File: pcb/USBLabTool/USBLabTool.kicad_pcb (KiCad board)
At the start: 4 copper layers, 79.4 x 56.2 mm, 227 parts, among them J1 Conn_01x06_Pin, J17 2x01, J19 T_N5V, J2 Conn_02x12_Odd_Even, J20 USB_C_Receptacle, K1 G5V-2, K2 G5V-2, Q1 STL11N3LLH6, SW1 TS02-66-73-BK-100-SCR-D, U1 AQY284SX, U10 MC33274ADR2G, U11 DG403, U12 STM32H562VGTx, U13 R1283K002A, U14 ST1L05APU33R, U15 ST1L05APU33R, U16 LTC1983ES6-5TRMPBF, U17 TCPP01-M12, U18 74HC245, U19 USBLC6-2SC6, U2 AQY284SX, U20 74HC245, U3 CD74HC4316, U4 LMP7718, U5 CD74HC4316, U6 LMP7718, U7 OPA863, U8 OPA863, U9 MC33274ADR2G, Y1 32.768kHz, Y2 NX2016SA-25M-EXS00A-CS08742

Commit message: push new layout
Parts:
- added JP3: SJ, Jumper:SolderJumper-2_P1.3mm_Open_RoundedPad1.0x1.5mm, F.Cu at (78.8, 90.0)
- added JP4: SJ, Jumper:SolderJumper-2_P1.3mm_Open_RoundedPad1.0x1.5mm, F.Cu at (74.1, 98.0)
- added JP5: SJ, Jumper:SolderJumper-2_P1.3mm_Open_RoundedPad1.0x1.5mm, F.Cu at (74.0, 95.3)
- added JP6: SJ, Jumper:SolderJumper-2_P1.3mm_Open_RoundedPad1.0x1.5mm, F.Cu at (196.4, 86.9)
- added JP7: SJ, Jumper:SolderJumper-2_P1.3mm_Open_RoundedPad1.0x1.5mm, F.Cu at (196.4, 90.5)
- added R82: 0, Resistor_SMD:R_0603_1608Metric_Pad0.98x0.95mm_HandSolder, F.Cu at (200.8, 86.4)
- added R83: 0, Resistor_SMD:R_0603_1608Metric_Pad0.98x0.95mm_HandSolder, F.Cu at (200.8, 88.9)
- C10, C11, C14, C22, C24, C26, C28, C31, C32, C35, C36, C37, C38, C40, C42, C45, C47, C50, C51, C54, C57, C58, C63, C64, C65, C67, C68, C71, C74, C75, C9, CR2, D10, D4, D5, D6, D9, L7, L8, R11, R13, R14, R15, R16, R17, R18, R19, R20, R23, R32, R35, R37, R56, R57, R59, R60, R61, R65, R68, R69, R70, R71, R72, R73, R74, R75, R76, R77, R78, R79, R80, R81, R9, U1, U13, U14, U15, U17, U19, U3, U8, Y1: moved to F.Cu
- C29, C3, C43, C44, C49, D1, R33, R43, R44, R45, R46, R49, R50, R52, U12: moved to B.Cu
- moved L6 128.7 mm to (58.4, 112.7), turned to 0 degrees
- moved H2 107.6 mm to (198.7, 53.7)
- moved R8 104.9 mm to (86.8, 131.2), turned to 90 degrees
- moved C8 102.9 mm to (88.3, 131.2), turned to -90 degrees
- moved C7 102.7 mm to (89.8, 131.2), turned to 90 degrees
- moved R7 102.1 mm to (91.3, 131.2), turned to -90 degrees
- moved C6 99.6 mm to (94.9, 131.2), turned to -90 degrees
- moved C5 99.4 mm to (98.0, 131.2), turned to 90 degrees
- moved C63 99.3 mm to (85.5, 95.8), turned to -90 degrees
- moved C62 99.2 mm to (89.7, 98.6), turned to 0 degrees
- moved R6 99.0 mm to (96.4, 131.2), turned to -90 degrees
- moved D2 98.9 mm to (108.6, 138.1), turned to -90 degrees
- moved J19 98.4 mm to (82.1, 97.2)
- moved C64 97.6 mm to (86.2, 98.5), turned to 0 degrees
- moved R5 97.2 mm to (99.5, 131.2), turned to 90 degrees
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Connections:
- C33 pad 1: RCC_OSC_IN -> Net-(JP6-B)
- C34 pad 2: RCC_OSC_OUT -> Net-(JP7-A)
- C35 pad 2: RCC_OSC32_IN -> Net-(C35-Pad2)
- C36 pad 2: RCC_OSC32_OUT -> Net-(C36-Pad2)
- C70 pad 1: +5V -> Net-(D10-A)
- C72 pad 2: UCPD_CC1 -> Net-(J20-CC1)
- C73 pad 2: UCPD_CC2 -> Net-(J20-CC2)
- C74 pad 2: +5V -> Net-(D10-A)
- D10 pad 2: +5V -> Net-(D10-A)
- D3 pad 1: +3.3VA -> GNDA
- D3 pad 2: GNDA -> +3.3VA
- D4 pad 1: +3.3VA -> GNDA
- D4 pad 2: GNDA -> +3.3VA
- D9 pad C: +5V -> Net-(D10-A)
- J20 pad A4: +5V -> Net-(D10-A)
- J20 pad A5: UCPD_CC1 -> Net-(J20-CC1)
- J20 pad A9: +5V -> Net-(D10-A)
- J20 pad B4: +5V -> Net-(D10-A)
- J20 pad B5: UCPD_CC2 -> Net-(J20-CC2)
- J20 pad B9: +5V -> Net-(D10-A)
- Q1 pad 5: +5V -> Net-(D10-A)
- R67 pad 1: +5V -> Net-(D10-A)
- U12 pad 70: USB_D- -> USB_FN_N
- U12 pad 71: USB_D+ -> USB_FN_P
- U17 pad 7: UCPD_CC1 -> Net-(J20-CC1)
- U17 pad 9: UCPD_CC2 -> Net-(J20-CC2)
- Y1 pad 1: RCC_OSC32_OUT -> Net-(C36-Pad2)
- Y1 pad 2: RCC_OSC32_IN -> Net-(C35-Pad2)
- Y2 pad 1: RCC_OSC_IN -> Net-(JP6-B)
- Y2 pad 3: RCC_OSC_OUT -> Net-(JP7-A)
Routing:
- net +5V: track 252.2 -> 78.0 mm, vias 11 -> 6
- net GNDA: track 331.4 -> 181.8 mm, vias 26 -> 14
- net GND: track 272.4 -> 157.4 mm, vias 32 -> 16
- net +3.3V: track 141.5 -> 31.2 mm, vias 11 -> 2
- net NRST: track 86.7 -> 0.00 mm, vias 2 -> 0
- net -5VCLEAN: track 108.1 -> 31.5 mm
- net +5VCLEAN: track 94.1 -> 33.4 mm, vias 7 -> 4
- net C0_IN: track 53.1 -> 4.65 mm, vias 2 -> 0
- net CH0_ACDC: track 45.9 -> 1.32 mm, vias 3 -> 1
- net +12VA: track 81.2 -> 40.0 mm, vias 5 -> 2
- net UCPD_FLT: track 42.7 -> 2.58 mm, vias 4 -> 1
- net P_CH0_IN: track 51.7 -> 11.9 mm
- net USB_D-: track 50.6 -> 11.9 mm, vias 4 -> 2
- net -12VA: track 75.0 -> 37.2 mm, vias 9 -> 5
- net UCPD_CC2: track 55.7 -> 19.2 mm, vias 5 -> 2
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- removed copper zone on In1.Cu, net GND
- removed copper zone on In1.Cu, net GNDA
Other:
- board outline removed
- board text removed: "ECE USB Multi-Function Lab Instrument"
- board text removed: "RESET"

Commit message: pcb update
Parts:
- turned GD2 to 180 degrees
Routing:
- net P_CH0_IN: track 11.9 -> 0.00 mm
- net Net-(C7-Pad2): track 9.14 -> 16.8 mm
- net GNDA: track 181.8 -> 175.1 mm, vias 14 -> 13
- net Net-(C7-Pad1): track 4.29 -> 5.83 mm
- net /AWG_FrontEnd/C1_OUT_G: track 16.5 -> 15.5 mm
- net /AWG_FrontEnd/C0_FB: track 25.5 -> 24.8 mm
- net Net-(U11B-D2): track 7.71 -> 7.15 mm

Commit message: pcb updates
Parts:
- turned GD1 to 180 degrees
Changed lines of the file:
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@@
 	(footprint "userfp:GDT_SH_LTF"
 		(layer "F.Cu")
-		(at 125.8715 139.7615)
+		(at 125.8715 139.7615 180)
 		(tags "SH90 ")
 		(property "Reference" "GD1"
-			(at 0 0 0)
+			(at 0 0 180)
 			(unlocked yes)
 			(layer "F.SilkS")
@@
 		)
 		(property "Value" "GDT_SH90"
-			(at 0 0 0)
+			(at 0 0 180)
 			(unlocked yes)
 			(layer "F.Fab")
@@
 		(attr smd)
 		(fp_line
+			(start 1.22915 -2.7305)
+			(end -1.22915 -2.7305)
+			(stroke
+				(width 0.1524)
+				(type solid)
+			)
+			(layer "F.SilkS")
+		)
+		(fp_line
 			(start -1.22915 2.7305)
 			(end 1.22915 2.7305)
@@
 		)
 		(fp_line
-			(start 1.22915 -2.7305)
-			(end -1.22915 -2.7305)
-			(stroke
-				(width 0.1524)
-				(type solid)
-			)
-			(layer "F.SilkS")
+			(start 2.8575 2.8575)
+			(end -2.8575 2.8575)
+			(stroke
+				(width 0.1524)
+				(type solid)
+			)
+			(layer "F.CrtYd")
+		)
+		(fp_line
+			(start 2.8575 -2.8575)
+			(end 2.8575 2.8575)
+			(stroke
+				(width 0.1524)
+				(type solid)
+			)
+			(layer "F.CrtYd")
+		)
+		(fp_line
+			(start -2.8575 2.8575)
+			(end -2.8575 -2.8575)
+			(stroke
+				(width 0.1524)
+				(type solid)
+			)
+			(layer "F.CrtYd")
 		)
 		(fp_line
@@
 		)
 		(fp_line
-			(start -2.8575 2.8575)
-			(end -2.8575 -2.8575)
-			(stroke
-				(width 0.1524)
-				(type solid)
-			)
-			(layer "F.CrtYd")
-		)
-		(fp_line
-			(start 2.8575 -2.8575)
-			(end 2.8575 2.8575)
-			(stroke
-				(width 0.1524)
-				(type solid)
-			)
-			(layer "F.CrtYd")
-		)
-		(fp_line
-			(start 2.8575 2.8575)
-			(end -2.8575 2.8575)
-			(stroke
-				(width 0.1524)
-				(type solid)
-			)
-			(layer "F.CrtYd")
+			(start 2.2479 2.6035)
+			(end 2.2479 -2.6035)
+			(stroke
+				(width 0.0254)
+				(type solid)
+			)
+			(layer "F.Fab")
+		)
+		(fp_line
+			(start 2.2479 2.6035)
+			(end 2.2479 -2.6035)
+			(stroke
+				(width 0.0254)
+				(type solid)
+			)
+			(layer "F.Fab")
+		)
+		(fp_line
+			(start 2.2479 -2.6035)
+			(end 1.5367 -2.6035)
+			(stroke
+				(width 0.0254)
+				(type solid)
+			)
+			(layer "F.Fab")
+		)
+		(fp_line
+			(start 2.2479 -2.6035)
+			(end -2.2479 -2.6035)
+			(stroke
+				(width 0.0254)
+				(type solid)
+			)
+			(layer "F.Fab")
+		)
+		(fp_line
+			(start 1.5367 2.6035)
+			(end 2.2479 2.6035)
+			(stroke
+				(width 0.0254)
+				(type solid)
+			)
+			(layer "F.Fab")
+		)
+		(fp_line
+			(start 1.5367 -2.6035)
+			(end 1.5367 2.6035)
+			(stroke
+				(width 0.0254)
+				(type solid)
+			)
+			(layer "F.Fab")
+		)
+		(fp_line
+			(start -1.5367 2.6035)
+			(end -1.5367 -2.6035)
+			(stroke
+				(width 0.0254)
+				(type solid)
+			)
+			(layer "F.Fab")
+		)
+		(fp_line
+			(start -1.5367 -2.6035)
+			(end -2.2479 -2.6035)
+			(stroke
+				(width 0.0254)
+				(type solid)
+			)
+			(layer "F.Fab")
+		)
+		(fp_line
+			(start -2.2479 2.6035)
+			(end 2.2479 2.6035)
+			(stroke
+				(width 0.0254)
+				(type solid)
+			)
+			(layer "F.Fab")
+		)
+		(fp_line
+			(start -2.2479 2.6035)
+			(end -1.5367 2.6035)
+			(stroke
+				(width 0.0254)
+				(type solid)
+			)
+			(layer "F.Fab")
 		)
 		(fp_line
@@
 			(start -2.2479 -2.6035)
 			(end -2.2479 2.6035)
-			(stroke
-				(width 0.0254)
-				(type solid)
-			)
-			(layer "F.Fab")
-		)
-		(fp_line
-			(start -2.2479 2.6035)
-			(end -1.5367 2.6035)
-			(stroke
-				(width 0.0254)
-				(type solid)
-			)
-			(layer "F.Fab")
-		)
-		(fp_line
-			(start -2.2479 2.6035)
-			(end 2.2479 2.6035)
-			(stroke
-				(width 0.0254)
-				(type solid)
-			)
-			(layer "F.Fab")
-		)
-		(fp_line
-			(start -1.5367 -2.6035)
-			(end -2.2479 -2.6035)
-			(stroke
-				(width 0.0254)
-				(type solid)
-			)
-			(layer "F.Fab")
-		)
-		(fp_line
-			(start -1.5367 2.6035)
-			(end -1.5367 -2.6035)
-			(stroke
-				(width 0.0254)
-				(type solid)
-			)
-			(layer "F.Fab")
-		)
-		(fp_line
-			(start 1.5367 -2.6035)
-			(end 1.5367 2.6035)
-			(stroke
-				(width 0.0254)
-				(type solid)
-			)
-			(layer "F.Fab")
-		)
-		(fp_line
-			(start 1.5367 2.6035)
-			(end 2.2479 2.6035)
-			(stroke
-				(width 0.0254)
-				(type solid)
-			)
-			(layer "F.Fab")
-		)
-		(fp_line
-			(start 2.2479 -2.6035)
-			(end -2.2479 -2.6035)
-			(stroke
-				(width 0.0254)
-				(type solid)
-			)
-			(layer "F.Fab")
-		)
-		(fp_line
-			(start 2.2479 -2.6035)
-			(end 1.5367 -2.6035)
-			(stroke
-				(width 0.0254)
-				(type solid)
-			)
-			(layer "F.Fab")
-		)
-		(fp_line
-			(start 2.2479 2.6035)
-			(end 2.2479 -2.6035)
-			(stroke
-				(width 0.0254)
-				(type solid)
-			)
-			(layer "F.Fab")
-		)
-		(fp_line
-			(start 2.2479 2.6035)
-			(end 2.2479 -2.6035)
 			(stroke
 				(width 0.0254)
@@
 		)
 		(fp_text user "${REFERENCE}"
-			(at 0 0 0)
+			(at 0 0 180)
 			(unlocked yes)
 			(layer "F.Fab")
@@
 		)
 		(pad "1" smd rect
-			(at -2.0701 0)
+			(at -2.0701 0 180)
 			(size 1.0668 5.207)
 			(layers "F.Cu" "F.Mask" "F.Paste")
@@
 		)
 		(pad "2" smd rect
-			(at 2.0701 0)
+			(at 2.0701 0 180)
 			(size 1.0668 5.207)
 			(layers "F.Cu" "F.Mask" "F.Paste")
@@
 			(polygon
 				(pts
-					(xy 124.3856 137.2088) (xy 127.3574 137.2088) (xy 127.3574 142.3142) (xy 124.3856 142.3142)
-				)
-			)
+					(xy 127.3574 142.3142) (xy 124.3856 142.3142) (xy 124.3856 137.2088) (xy 127.3574 137.2088)
+				)
+			)

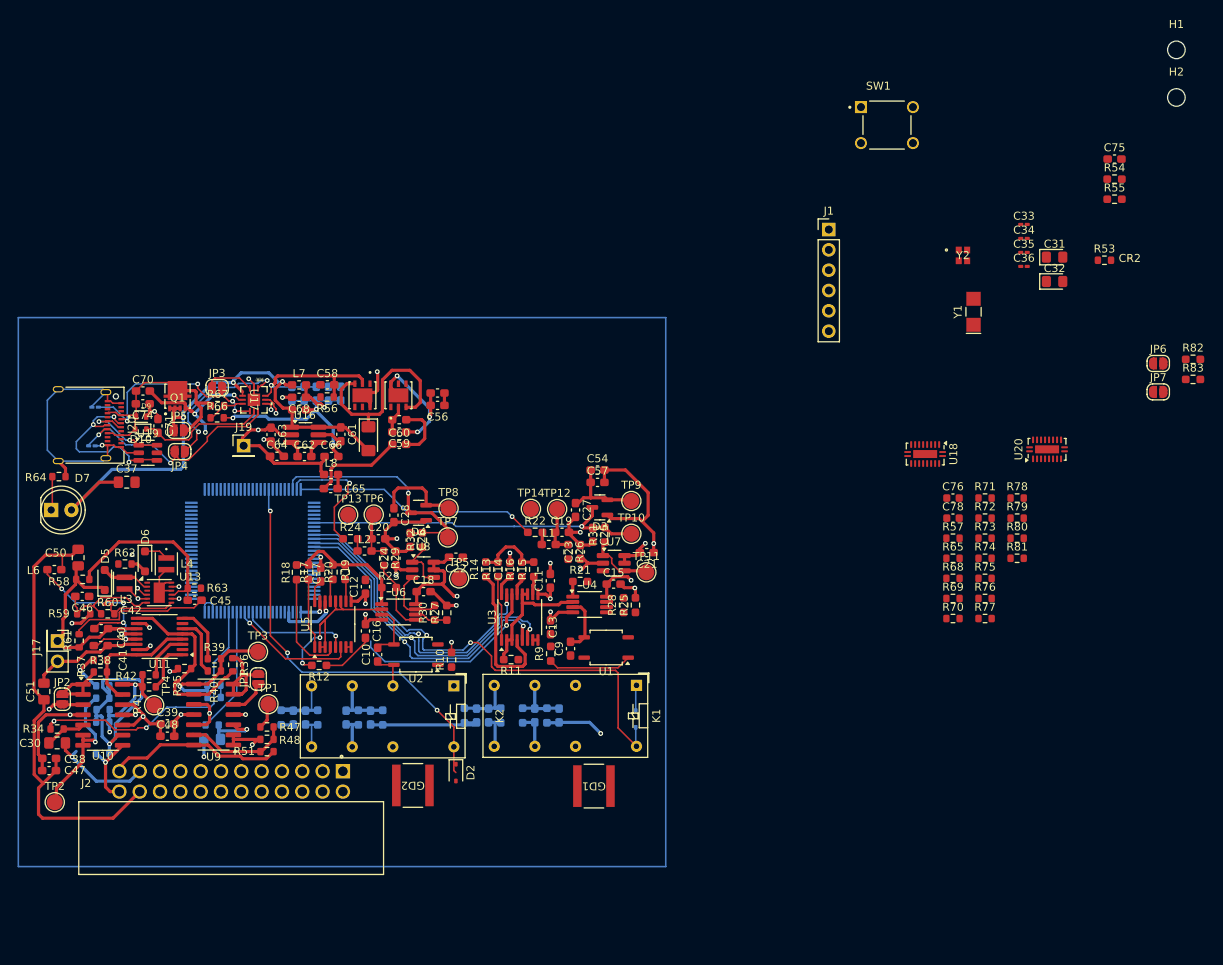
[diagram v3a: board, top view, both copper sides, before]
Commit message: change MCU pads and add ground planes and power planes
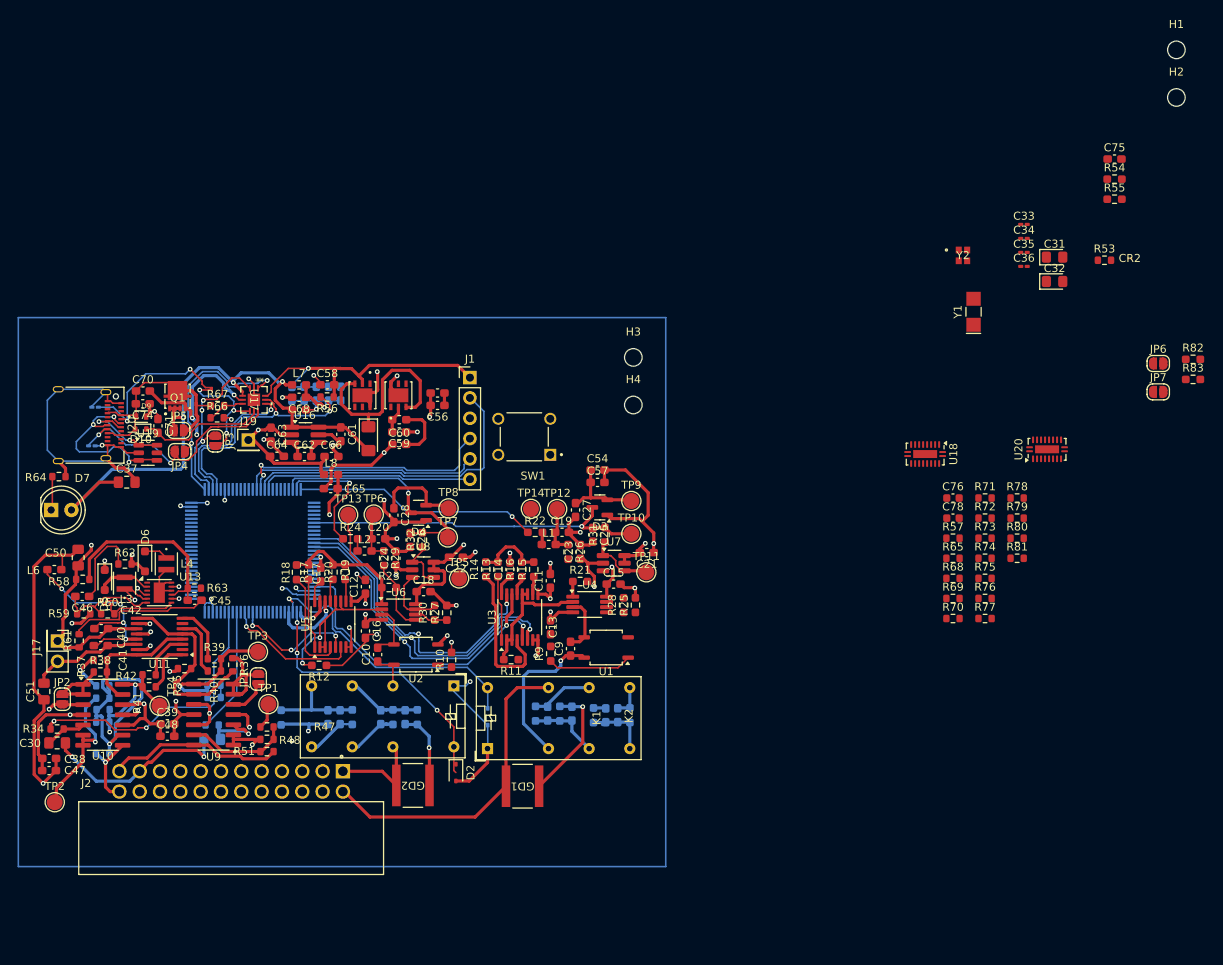
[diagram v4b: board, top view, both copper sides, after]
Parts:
- added H3: MountingHole, MountingHole:MountingHole_2.2mm_M2, F.Cu at (130.8, 86.2)
- added H4: MountingHole, MountingHole:MountingHole_2.2mm_M2, F.Cu at (130.8, 92.1)
- moved SW1 59.8 mm to (117.2, 96.1), turned to 180 degrees
- moved J1 48.5 mm to (110.4, 88.7)
- moved K1 20.2 mm to (112.6, 135.1), turned to 90 degrees
- moved D1 18.5 mm to (112.6, 131.1), turned to -90 degrees
- moved C3 16.1 mm to (128.8, 130.9), turned to -90 degrees
- moved C4 16.1 mm to (127.3, 130.9), turned to 90 degrees
- moved R1 16.1 mm to (130.4, 130.9), turned to 90 degrees
- moved R2 16.1 mm to (125.8, 130.9), turned to -90 degrees
- moved GD1 8.92 mm to (117.0, 139.8)
- moved JP3 6.65 mm to (78.5, 96.6), turned to -90 degrees
- moved R5 4.33 mm to (103.8, 131.1)
- moved R6 4.33 mm to (100.8, 131.1)
- moved R7 4.33 mm to (95.7, 131.1)
- moved C5 4.33 mm to (102.3, 131.2)
- moved C6 4.33 mm to (99.2, 131.2)
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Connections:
- U12 pad 1: unconnected-(U12-PE2-Pad1) -> UCPD_CC2
- U12 pad 15: unconnected-(U12-PC0-Pad15) -> DEBUG_JTMS-SWDI0
- U12 pad 16: unconnected-(U12-PC1-Pad16) -> DEBUG_JTCK_SWCLK
- U12 pad 17: CH0_attenuate -> DEBUG_JTD-SW0
- U12 pad 2: unconnected-(U12-PE3-Pad2) -> UCPD_CC1
- U12 pad 3: unconnected-(U12-PE4-Pad3) -> USCPD_DBn
- U12 pad 34: CH1_attenuate -> unconnected-(U12-PC5-Pad34)
- U12 pad 4: unconnected-(U12-PE5-Pad4) -> UCPD_FLT
- U12 pad 52: UCPD_CC1 -> CH0_attenuate
- U12 pad 53: UCPD_CC2 -> CH1_attenuate
- U12 pad 66: UCPD_FLT -> unconnected-(U12-PC9-Pad66)
- U12 pad 68: USCPD_DBn -> unconnected-(U12-PA9-Pad68)
- U12 pad 72: DEBUG_JTMS-SWDI0 -> unconnected-(U12-PA13(JTMS-Pad72)
- U12 pad 76: DEBUG_JTCK_SWCLK -> unconnected-(U12-PA14(JTCK-Pad76)
- U12 pad 89: DEBUG_JTD-SW0 -> unconnected-(U12-PB3(JTDO-Pad89)
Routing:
- net GND: track 157.4 -> 238.0 mm, vias 16 -> 23
- net GNDA: track 175.1 -> 235.6 mm, vias 13 -> 21
- net -5VCLEAN: track 31.5 -> 81.1 mm, vias 9 -> 11
- net P_CH1_IN: track 0.00 -> 40.1 mm
- net NRST: track 0.00 -> 40.0 mm
- net DEBUG_JTCK_SWCLK: track 0.00 -> 38.9 mm
- net DEBUG_JTMS-SWDI0: track 0.00 -> 32.5 mm, vias 0 -> 2
- net +3.3V: track 31.2 -> 62.2 mm, vias 2 -> 5
- net UCPD_FLT: track 2.58 -> 30.5 mm, vias 1 -> 2
- net CH1_attenuate: track 63.1 -> 36.5 mm, vias 2 -> 1
- net DEBUG_JTD-SW0: track 0.00 -> 26.6 mm
- net +5V: track 78.0 -> 101.6 mm
- net Net-(C9-Pad1): track 0.00 -> 19.5 mm, vias 0 -> 1
- net USCPD_DBn: track 1.33 -> 19.7 mm
- net CH0_attenuate: track 52.2 -> 35.4 mm
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- added copper zone on In2.Cu, net +12VA
- added copper zone on In2.Cu, net +3.3V
- added copper zone on In2.Cu, net +5V
- added copper zone on In2.Cu, net +5VCLEAN
- added copper zone on In2.Cu, net -12VA
- added copper zone on In2.Cu, net -5V
- added copper zone on In2.Cu, net -5VCLEAN
- added copper zone on In1.Cu, net GND
- added copper zone on In1.Cu, net GNDA

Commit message: reposition a few things
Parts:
- moved J1 54.0 mm to (58.0, 102.0), turned to 90 degrees
- moved D7 52.1 mm to (109.5, 97.1), turned to 180 degrees
- moved R64 48.9 mm to (106.4, 89.1), turned to 180 degrees
- moved C37 29.3 mm to (96.7, 99.8), turned to 180 degrees
- moved Y2 15.8 mm to (182.1, 85.6)
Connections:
- U12 pad 15: DEBUG_JTMS-SWDI0 -> unconnected-(U12-PC0-Pad15)
- U12 pad 16: DEBUG_JTCK_SWCLK -> unconnected-(U12-PC1-Pad16)
- U12 pad 17: DEBUG_JTD-SW0 -> unconnected-(U12-PC2-Pad17)
- U12 pad 72: unconnected-(U12-PA13(JTMS-Pad72) -> DEBUG_JTMS-SWDI0
- U12 pad 76: unconnected-(U12-PA14(JTCK-Pad76) -> DEBUG_JTCK_SWCLK
- U12 pad 89: unconnected-(U12-PB3(JTDO-Pad89) -> DEBUG_JTD-SW0
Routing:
- net GND: track 238.0 -> 220.7 mm, vias 23 -> 27
- net DEBUG_JTD-SW0: track 26.6 -> 10.9 mm
- net +3.3V: track 62.2 -> 72.6 mm
- net NRST: track 40.0 -> 30.4 mm, vias 0 -> 2
- net DEBUG_JTCK_SWCLK: track 38.9 -> 29.8 mm
- net DEBUG_JTMS-SWDI0: track 32.5 -> 23.3 mm
- net +5V: track 101.6 -> 95.2 mm, vias 6 -> 7
- net Net-(D6-K): track 3.04 -> 8.92 mm
- net Net-(D7-K): track 4.24 -> 8.99 mm
- net -12VA: track 40.9 -> 43.9 mm, vias 5 -> 6
- net GNDA: track 235.6 -> 233.6 mm, vias 21 -> 23
